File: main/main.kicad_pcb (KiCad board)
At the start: 2 copper layers, 61 x 38 mm, 94 parts, among them J1 enc_host, J2 enc_slave, J3 motor_L, J4 motor_R, J5 Battery, J6 enc_host, J7 enc_slave, J8 Conn_ARM_JTAG_SWD_10, Q1 LTR-209, Q2 IRLML6402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

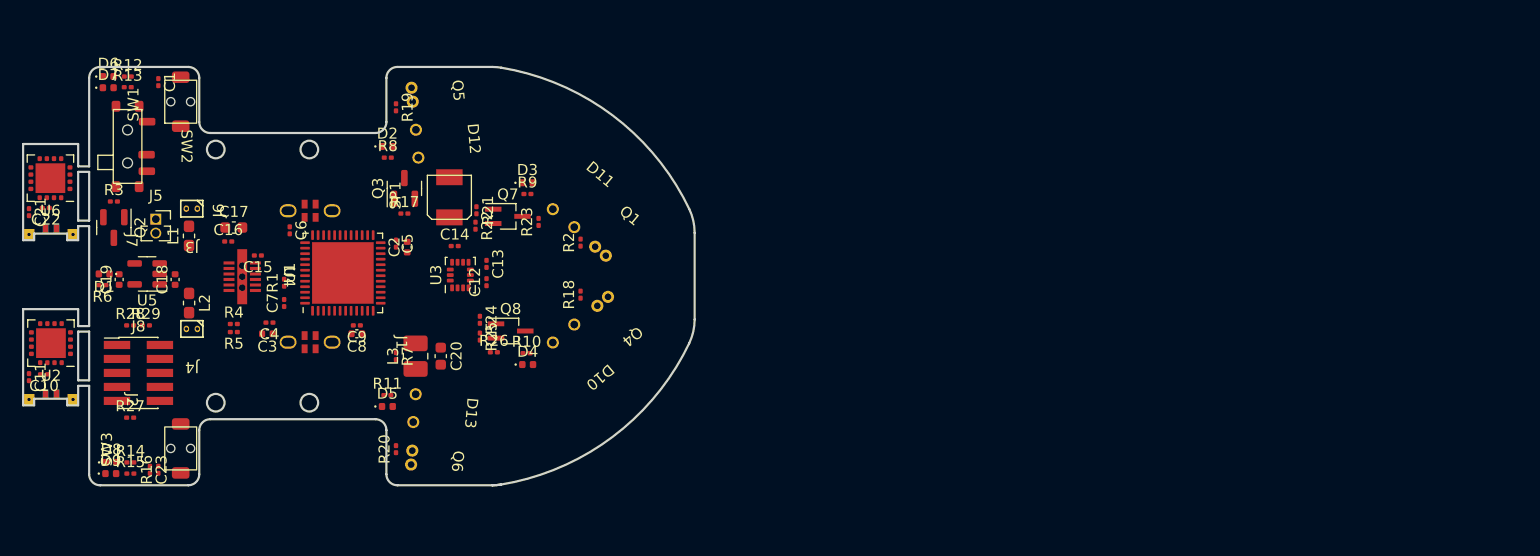
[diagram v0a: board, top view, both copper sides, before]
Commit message: feat: update main board
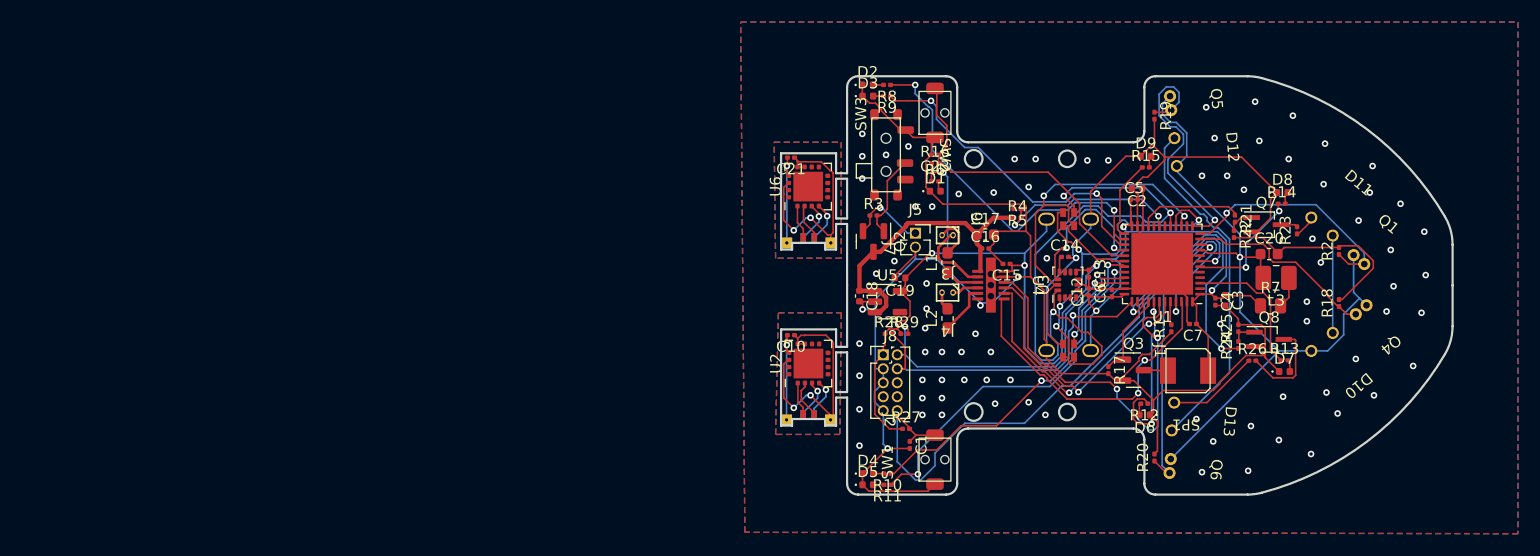
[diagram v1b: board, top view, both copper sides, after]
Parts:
- removed C11, C22: 0.1u, Capacitor_SMD:C_0201_0603Metric
- removed C8: 1u, Capacitor_SMD:C_0402_1005Metric
- removed C9: 0.01u, Capacitor_SMD:C_0201_0603Metric
- J8: footprint Connector_PinHeader_1.27mm:PinHeader_2x05_P1.27mm_Vertical_SMD -> Connector_PinHeader_1.27mm:PinHeader_2x05_P1.27mm_Vertical
- R7: footprint Resistor_SMD:R_0201_0603Metric -> Resistor_SMD:R_0805_2012Metric
- moved D7 109.9 mm to (184.4, 105.0)
- moved D8 109.2 mm to (184.2, 88.8)
- moved R13 108.0 mm to (184.4, 104.0)
- moved R14 107.2 mm to (184.2, 89.8)
- moved D6 99.0 mm to (171.7, 109.0), turned to 180 degrees
- moved D9 98.3 mm to (171.8, 85.5)
- moved R12 97.0 mm to (171.7, 108.0), turned to 180 degrees
- moved R15 96.3 mm to (171.8, 86.5)
- moved C3 87.1 mm to (179.0, 98.6), turned to -90 degrees
- moved C4 85.9 mm to (178.1, 98.7), turned to -90 degrees
- moved C7 82.6 mm to (176.1, 100.7), turned to 180 degrees
- moved R1 80.7 mm to (174.1, 101.1)
- moved R7 79.6 mm to (183.1, 99.1), turned to 0 degrees
- moved L3 78.5 mm to (183.6, 96.5), turned to 180 degrees
- moved C23 76.8 mm to (152.7, 85.3), turned to 180 degrees
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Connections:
- J1 pad 2: SPI_MOSI -> SPI_MISO
- J1 pad 3: SPI_MISO -> SPI_MOSI
- J1 pad 4: SPI_SCLK -> SPI_CS_ENC_R
- J1 pad 5: SPI_CS_ENC_R -> SPI_SCLK
- J2 pad 2: /encoder_R/s_MOSI -> /encoder_R/s_MISO
- J2 pad 3: /encoder_R/s_MISO -> /encoder_R/s_MOSI
- J2 pad 4: /encoder_R/s_SCK -> /encoder_R/s_CS
- J2 pad 5: /encoder_R/s_CS -> /encoder_R/s_SCK
- J6 pad 2: SPI_MOSI -> SPI_MISO
- J6 pad 3: SPI_MISO -> SPI_MOSI
- J6 pad 4: SPI_SCLK -> SPI_CS_ENC_L
- J6 pad 5: SPI_CS_ENC_L -> SPI_SCLK
- J7 pad 2: /encoder_L/s_MOSI -> /encoder_L/s_MISO
- J7 pad 3: /encoder_L/s_MISO -> /encoder_L/s_MOSI
- J7 pad 4: /encoder_L/s_SCK -> /encoder_L/s_CS
- J7 pad 5: /encoder_L/s_CS -> /encoder_L/s_SCK
- U1 pad 10: IR_RCV_FL -> IR_RCV_SR
- U1 pad 12: IR_RCV_SL -> IR_RCV_FL
- U1 pad 13: IR_RCV_SR -> IR_RCV_SL
- U1 pad 14: BAT_VOL -> unconnected-(U1-Pad14)
- U1 pad 18: SPI_CS_IMU -> unconnected-(U1-Pad18)
- U1 pad 19: SPI_CS_ENC_R -> BAT_VOL
- U1 pad 2: USER_LED5 -> unconnected-(U1-Pad2)
- U1 pad 20: SPI_CS_ENC_L -> unconnected-(U1-Pad20)
- U1 pad 21: unconnected-(U1-Pad21) -> IR_LED_F
- U1 pad 25: USER_LED1 -> USER_LED8
- U1 pad 26: USER_LED2 -> USER_LED1
- U1 pad 27: USER_LED3 -> USER_LED2
- U1 pad 28: USER_LED4 -> SPI_CS_IMU
- U1 pad 30: USART_TX -> SPI_CS_ENC_L
- U1 pad 31: USART_RX -> USER_LED3
- U1 pad 32: unconnected-(U1-Pad32) -> USER_LED4
- U1 pad 33: unconnected-(U1-Pad33) -> SPI_CS_ENC_R
- U1 pad 38: IR_LED_F -> unconnected-(U1-Pad38)
- U1 pad 4: USER_LED7 -> unconnected-(U1-Pad4)
- U1 pad 41: unconnected-(U1-Pad41) -> USER_LED5
- U1 pad 5: USER_LED8 -> unconnected-(U1-Pad5)
- U1 pad 6: unconnected-(U1-Pad6) -> USER_LED7
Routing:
- net GND: track 0.00 -> 247.8 mm, vias 0 -> 85
- net +3.3V: track 0.00 -> 126.2 mm, vias 0 -> 7
- net +3.3VADC: track 0.00 -> 66.2 mm, vias 0 -> 1
- net SPI_MOSI: track 0.00 -> 57.9 mm, vias 0 -> 3
- net NRST: track 0.00 -> 54.0 mm, vias 0 -> 1
- net MOTOR_IN_R1: track 0.00 -> 40.8 mm, vias 0 -> 2
- net MOTOR_IN_L1: track 0.00 -> 36.2 mm, vias 0 -> 2
- net SPI_SCLK: track 0.00 -> 35.7 mm, vias 0 -> 2
- net SPI_MISO: track 0.00 -> 34.7 mm, vias 0 -> 4
- net USER_LED4: track 0.00 -> 33.0 mm, vias 0 -> 2
- net USER_LED1: track 0.00 -> 33.0 mm, vias 0 -> 2
- net USER_LED3: track 0.00 -> 32.2 mm, vias 0 -> 2
- net Net-(D12-Pad1): track 0.00 -> 31.9 mm
- net SYS_JTCK_SWCLK: track 0.00 -> 30.5 mm, vias 0 -> 1
- net SYS_JTMS_SWDIO: track 0.00 -> 29.9 mm, vias 0 -> 2
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- added copper zone on B.Cu, net /encoder_L/s_GND
- added copper zone on F.Cu, net /encoder_L/s_GND
- added copper zone on B.Cu, net /encoder_R/s_GND
- added copper zone on F.Cu, net /encoder_R/s_GND
- added copper zone on B.Cu, net GND
- added copper zone on F.Cu, net GND
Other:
- outline, holes or cut-outs redrawn
